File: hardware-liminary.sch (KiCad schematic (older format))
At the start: 51 parts, among them J1 Conn_01x05, J2 Conn_01x03, J3 Conn_01x03, J4 Conn_02x05_Odd_Even, J5 Conn_01x02, J6 UFL Conn, K1 HL2-1CH-12S, Q1 CMBT3904, Q2 PT204-6C, Q3 CMBT2222A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

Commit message: Asociadas footprint de componentes standard
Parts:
- AE1: footprint (none) -> Connector_Pin:Pin_D1.3mm_L11.0mm_LooseFit
- BAT1, J5, JP1: footprint (none) -> Connector_PinHeader_2.54mm:PinHeader_1x02_P2.54mm_Vertical
- C1: footprint (none) -> Capacitor_THT:CP_Radial_D5.0mm_P2.00mm
- C10: footprint (none) -> Capacitor_SMD:C_1206_3216Metric_Pad1.42x1.75mm_HandSolder
- C11, C12, C13, C2, C9: footprint (none) -> Capacitor_SMD:C_0805_2012Metric_Pad1.15x1.40mm_HandSolder
- C14, C3, C5, C6, C7, C8: footprint (none) -> Capacitor_SMD:CP_Elec_4x5.3
- C4: footprint (none) -> Capacitor_SMD:CP_Elec_4x5.4
- J1: footprint (none) -> Connector_PinHeader_2.54mm:PinHeader_1x05_P2.54mm_Vertical
- J2, J3: footprint (none) -> Connector_PinHeader_2.54mm:PinHeader_1x03_P2.54mm_Vertical
- J4: footprint (none) -> Connector_PinHeader_1.27mm:PinHeader_2x05_P1.27mm_Vertical
- J6: footprint TE_1909763-1 -> (none)
- K1: footprint Relay_THT:Relay_StandexMeder_DIP_LowProfile -> (none)
- LED1: footprint LED_SMD:LED_LiteOn_LTST-S326 -> (none)
- PS1: footprint Converter_ACDC:Converter_ACDC_MeanWell_IRM-03-xx_THT -> (none)
- Q1, Q3: footprint Package_TO_SOT_SMD:SOT-23 -> (none)
- Q2: footprint (none) -> LED_THT:LED_D5.0mm_Clear
- R1, R10, R11, R2, R3, R4, R5, R6, R7, R8, R9: footprint (none) -> Resistor_SMD:R_1206_3216Metric_Pad1.42x1.75mm_HandSolder
- RV1: footprint (none) -> Varistor:RV_Disc_D15.5mm_W3.9mm_P7.5mm
- U1: footprint lib:EESAMR34 -> (none)
- U2: footprint Package_TO_SOT_SMD:SOT-223-3_TabPin2 -> (none)

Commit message: eesam34
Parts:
- removed J6: UFL Conn, symbol 1909763-1:1909763-1
- removed LED1: 12-22/G6R6C-A31/2C, symbol LED_12-22:12-22SURSYGC_S530-A2_TR8
- removed U1: EESAMR34J18-V1_CT, symbol EESAMR34:EESAMR34J18-V1_CT
- removed U6: MCP6001T-I_OT, symbol MCP6001T-I_OT:MCP6001T-I_OT
- added U1: EESAMR34J18-V1_CT, proyect_EESAMR34:EESAMR34, symbol proyect_EESAMR34J18-V1_CT:EESAMR34J18-V1_CT
- JP3, JP4: footprint (none) -> Resistor_SMD:R_1206_3216Metric_Pad1.42x1.75mm_HandSolder
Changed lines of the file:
@@
 	3100 1350 3100 1250
-$Comp
-L MCP6001T-I_OT:MCP6001T-I_OT U6
-U 1 1 5F764C68
-P 3550 3500
-F 0 "U6" H 4150 3350 50  0000 C CNN
-F 1 "MCP6001T-I_OT" H 4150 3250 50  0000 C CNN
-F 2 "" H 4600 3900 50  0001 L CNN
-F 3 "http://docs-emea.rs-online.com/webdocs/0dd1/0900766b80dd189c.pdf" H 4600 3800 50  0001 L CNN
-F 4 "Single 1.8V Op Amp, 1MHz, I temp" H 4600 3700 50  0001 L CNN "Description"
-F 5 "1.45" H 4600 3600 50  0001 L CNN "Height"
-F 6 "Microchip" H 4600 3500 50  0001 L CNN "Manufacturer_Name"
-F 7 "MCP6001T-I/OT" H 4600 3400 50  0001 L CNN "Manufacturer_Part_Number"
-F 8 "MCP6001T-I/OT" H 4600 3300 50  0001 L CNN "Arrow Part Number"
-F 9 "https://www.arrow.com/en/products/mcp6001t-iot/microchip-technology" H 4600 3200 50  0001 L CNN "Arrow Price/Stock"
-F 10 "579-MCP6001T-I/OT" H 4600 3100 50  0001 L CNN "Mouser Part Number"
-F 11 "https://www.mouser.co.uk/ProductDetail/Microchip-Technology/MCP6001T-I-OT?qs=Q%2Fw7XRh99iki9dglS7IqJg%3D%3D" H 4600 3000 50  0001 L CNN "Mouser Price/Stock"
-	1    3550 3500
-	-1   0    0    -1
-$EndComp
 $Comp
 L Device:R R7
@@
 Wire Notes Line
 	5800 2400 500  2400
-$Comp
-L EESAMR34:EESAMR34J18-V1_CT U1
-U 1 1 5F95A58C
-P 2000 6650
-F 0 "U1" H 2150 6700 50  0000 R CNN
-F 1 "EESAMR34J18-V1_CT" H 2500 6550 50  0000 R CNN
-F 2 "" H 2000 6650 50  0001 L BNN
-F 3 "" H 2000 6650 118 0001 C CNN
-	1    2000 6650
-	1    0    0    -1
-$EndComp
 $Comp
 L power:GNDD #PWR0103
@@
 	1800 7650 1800 8150
 $Comp
-L LED_12-22:12-22SURSYGC_S530-A2_TR8 LED1
-U 1 1 5F8C80DF
-P 4500 8150
-F 0 "LED1" H 5000 8415 50  0000 C CNN
-F 1 "12-22/G6R6C-A31/2C" H 5000 8324 50  0000 C CNN
-F 2 "" H 5350 8250 50  0001 L CNN
-F 3 "" H 5350 8150 50  0001 L CNN
-F 4 "" H 5350 8050 50  0001 L CNN "Description"
-F 5 "2.2" H 5350 7950 50  0001 L CNN "Height"
-F 6 "Everlight" H 5350 7850 50  0001 L CNN "Manufacturer_Name"
-F 7 "12-22SURSYGC/S530-A2/TR8" H 5350 7750 50  0001 L CNN "Manufacturer_Part_Number"
-F 8 "12-22SURSYGC/S530-A2/TR8" H 5350 7650 50  0001 L CNN "Arrow Part Number"
-F 9 "" H 5350 7550 50  0001 L CNN "Arrow Price/Stock"
-F 10 "638-1222SURSYGCA2TR8" H 5350 7450 50  0001 L CNN "Mouser Part Number"
-F 11 "https://www.mouser.com/Search/Refine.aspx?Keyword=638-1222SURSYGCA2TR8" H 5350 7350 50  0001 L CNN "Mouser Price/Stock"
-	1    4500 8150
-	-1   0    0    -1
-$EndComp
-$Comp
 L Device:R R11
 U 1 1 5F8CC602
@@
 Antenna
 $Comp
-L 1909763-1:1909763-1 J6
-U 1 1 5FA17C3E
-P 6900 6000
-F 0 "J6" H 7188 6040 50  0000 L CNN
-F 1 "UFL Conn" H 7188 5949 50  0000 L CNN
-F 2 "" H 6900 6000 50  0001 L BNN
-F 3 "1909763-1" H 6900 6000 50  0001 L BNN
-F 4 "1" H 6900 6000 50  0001 L BNN "Field4"
-	1    6900 6000
-	1    0    0    -1
-$EndComp
-$Comp
 L power:GNDD #PWR014
 U 1 1 5FA23786
@@
 F 0 "JP4" H 6400 6164 50  0000 C CNN
 F 1 "Jumper" H 6400 6073 50  0000 C CNN
-F 2 "" H 6400 5900 50  0001 C CNN
+F 2 "Resistor_SMD:R_1206_3216Metric_Pad1.42x1.75mm_HandSolder" H 6400 5900 50  0001 C CNN
 F 3 "~" H 6400 5900 50  0001 C CNN
 	1    6400 5900
@@
 F 0 "JP3" H 6400 5814 50  0000 C CNN
 F 1 "Jumper" H 6400 5723 50  0000 C CNN
-F 2 "" H 6400 5550 50  0001 C CNN
+F 2 "Resistor_SMD:R_1206_3216Metric_Pad1.42x1.75mm_HandSolder" H 6400 5550 50  0001 C CNN
 F 3 "~" H 6400 5550 50  0001 C CNN
 	1    6400 5550
@@
 Wire Notes Line
 	7750 2350 7750 500
+$Comp
+L proyect_EESAMR34J18-V1_CT:EESAMR34J18-V1_CT U1
+U 1 1 5F767C93
+P 2000 6650
+F 0 "U1" H 1057 6646 50  0000 R CNN
+F 1 "EESAMR34J18-V1_CT" H 1057 6555 50  0000 R CNN
+F 2 "proyect_EESAMR34:EESAMR34" H 2000 6650 50  0001 L BNN
+F 3 "" H 2000 6650 50  0001 C CNN
+	1    2000 6650
+	1    0    0    -1
+$EndComp
 $EndSCHEMATC

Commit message: opAmp
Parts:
- added IC1: MCP6001T-I_OT, proyect_MCP6001T-I_OT:SOT95P270X145-5N, symbol proyect_MCP6001T-I_OT:MCP6001T-I_OT
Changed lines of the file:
@@
 	1    0    0    -1
 $EndComp
+$Comp
+L proyect_MCP6001T-I_OT:MCP6001T-I_OT IC1
+U 1 1 5F79C962
+P 3550 3500
+F 0 "IC1" H 4150 4281 50  0000 C CNN
+F 1 "MCP6001T-I_OT" H 4150 4190 50  0000 C CNN
+F 2 "proyect_MCP6001T-I_OT:SOT95P270X145-5N" H 4600 3900 50  0001 L CNN
+F 3 "http://docs-emea.rs-online.com/webdocs/0dd1/0900766b80dd189c.pdf" H 4600 3800 50  0001 L CNN
+F 4 "Single 1.8V Op Amp, 1MHz, I temp" H 4600 3700 50  0001 L CNN "Description"
+F 5 "1.45" H 4600 3600 50  0001 L CNN "Height"
+F 6 "Microchip" H 4600 3500 50  0001 L CNN "Manufacturer_Name"
+F 7 "MCP6001T-I/OT" H 4600 3400 50  0001 L CNN "Manufacturer_Part_Number"
+F 8 "MCP6001T-I/OT" H 4600 3300 50  0001 L CNN "Arrow Part Number"
+F 9 "https://www.arrow.com/en/products/mcp6001t-iot/microchip-technology" H 4600 3200 50  0001 L CNN "Arrow Price/Stock"
+F 10 "579-MCP6001T-I/OT" H 4600 3100 50  0001 L CNN "Mouser Part Number"
+F 11 "https://www.mouser.co.uk/ProductDetail/Microchip-Technology/MCP6001T-I-OT?qs=Q%2Fw7XRh99iki9dglS7IqJg%3D%3D" H 4600 3000 50  0001 L CNN "Mouser Price/Stock"
+	1    3550 3500
+	-1   0    0    -1
+$EndComp
 $EndSCHEMATC

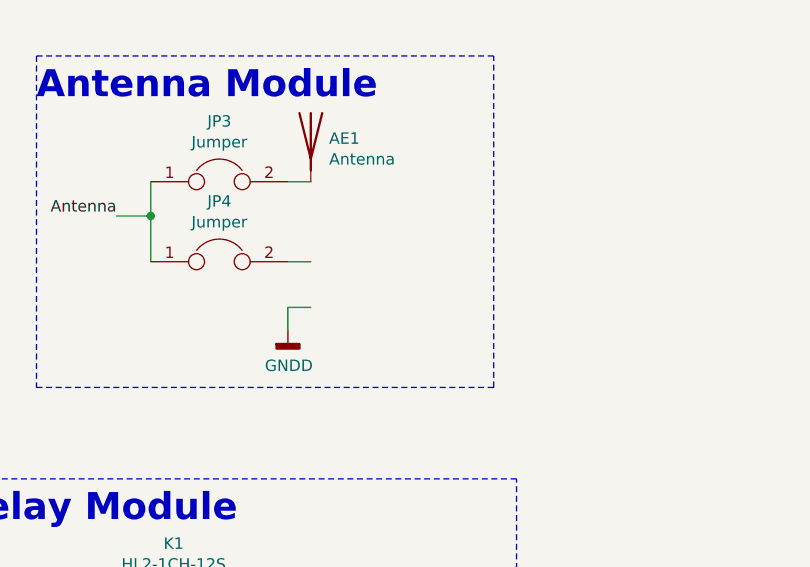
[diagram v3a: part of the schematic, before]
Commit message: ufl connector
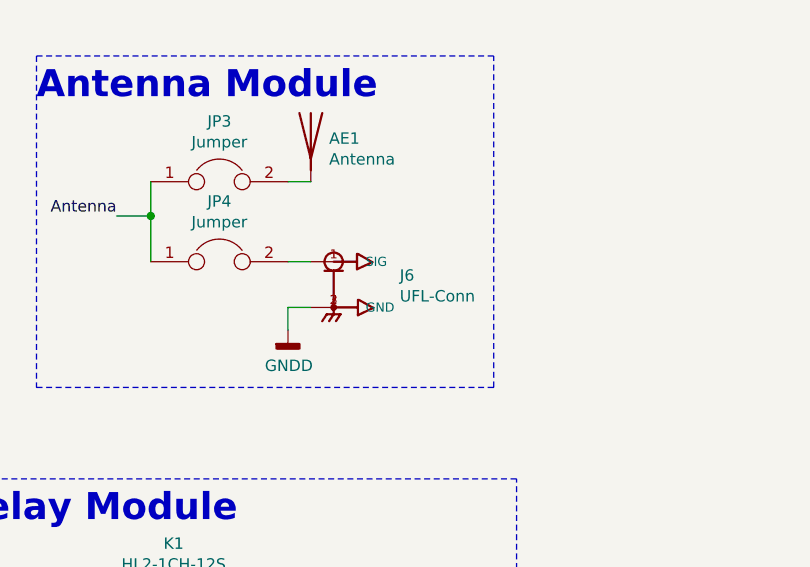
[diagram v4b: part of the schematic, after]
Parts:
- added J6: UFL-Conn, proyect_UFL-Conn:TE_1909763-1, symbol proyect_UFL-Conn:1909763-1
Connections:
- net GNDD: now also J6.2 (GND), J6.3 (GND)
- net at JP4.2: now also J6.1 (SIG)
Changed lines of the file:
@@
 	-1   0    0    -1
 $EndComp
+$Comp
+L proyect_UFL-Conn:1909763-1 J6
+U 1 1 5F7BE21B
+P 6900 6000
+F 0 "J6" H 7189 6040 50  0000 L CNN
+F 1 "UFL-Conn" H 7189 5949 50  0000 L CNN
+F 2 "proyect_UFL-Conn:TE_1909763-1" H 6900 6000 50  0001 L BNN
+F 3 "1909763-1" H 6900 6000 50  0001 L BNN
+F 4 "1" H 6900 6000 50  0001 L BNN "Field4"
+	1    6900 6000
+	1    0    0    -1
+$EndComp
 $EndSCHEMATC

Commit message: power supply
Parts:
- removed PS1: IRM-03-12, symbol Converter_ACDC:IRM-03-12
- added PS1: IRM-03-12, proyect_IRM-03-12:IRM0312, symbol proyect_IRM-03-12:IRM-03-12
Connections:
- net +12v: now also PS1.5 (+V)
- net GNDA: now also PS1.4 (-V)
- net Linea: now also PS1.1 (AC/L)
- net Neutro: now also PS1.2 (AC/N)
- no-connect marks 22 -> 24
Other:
- moved on the sheet: RV1
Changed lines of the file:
@@
 L Device:Varistor RV1
 U 1 1 5F736B9D
-P 3100 1100
-F 0 "RV1" H 2979 1054 50  0000 R CNN
-F 1 "Varistor" H 2979 1145 50  0000 R CNN
-F 2 "Varistor:RV_Disc_D15.5mm_W3.9mm_P7.5mm" V 3030 1100 50  0001 C CNN
-F 3 "~" H 3100 1100 50  0001 C CNN
-	1    3100 1100
+P 2450 1100
+F 0 "RV1" H 2329 1054 50  0000 R CNN
+F 1 "Varistor" H 2329 1145 50  0000 R CNN
+F 2 "Varistor:RV_Disc_D15.5mm_W3.9mm_P7.5mm" V 2380 1100 50  0001 C CNN
+F 3 "~" H 2450 1100 50  0001 C CNN
+	1    2450 1100
 	1    0    0    1
 $EndComp
@@
 Wire Wire Line
 	3400 2000 3400 2050
-Text Label 2700 850  2    50   ~ 0
+Text Label 2050 850  2    50   ~ 0
 Linea
-Text Label 2700 1350 2    50   ~ 0
+Text Label 2050 1350 2    50   ~ 0
 Neutro
 Wire Wire Line
-	2700 850  3100 850
-Wire Wire Line
-	3100 850  3100 950
-Wire Wire Line
-	2700 1350 3100 1350
-Wire Wire Line
-	3100 1350 3100 1250
+	2050 850  2450 850
+Wire Wire Line
+	2450 850  2450 950
+Wire Wire Line
+	2050 1350 2450 1350
+Wire Wire Line
+	2450 1350 2450 1250
 $Comp
 L Device:R R7
@@
 Wire Wire Line
 	4600 7700 4600 7800
-$Comp
-L Converter_ACDC:IRM-03-12 PS1
-U 1 1 5F9364C1
-P 3700 1100
-F 0 "PS1" H 3700 1467 50  0000 C CNN
-F 1 "IRM-03-12" H 3700 1376 50  0000 C CNN
-F 2 "" H 3700 750 50  0001 C CNN
-F 3 "https://www.meanwell.com/Upload/PDF/IRM-03/IRM-03-SPEC.PDF" H 3700 700 50  0001 C CNN
-	1    3700 1100
-	1    0    0    -1
-$EndComp
-Wire Wire Line
-	3300 1000 3300 850
-Wire Wire Line
-	3300 850  3100 850
-Connection ~ 3100 850
-Wire Wire Line
-	3300 1200 3300 1350
-Wire Wire Line
-	3300 1350 3100 1350
-Connection ~ 3100 1350
-Wire Wire Line
-	4100 1200 4100 1300
+Wire Wire Line
+	2650 850  2450 850
+Connection ~ 2450 850
+Wire Wire Line
+	2650 1350 2450 1350
+Connection ~ 2450 1350
 Wire Wire Line
 	4100 1300 4300 1300
 Connection ~ 4300 1300
-Wire Wire Line
-	4100 1000 4100 900
 Wire Wire Line
 	4100 900  4300 900
@@
 	1    0    0    -1
 $EndComp
+$Comp
+L proyect_IRM-03-12:IRM-03-12 PS1
+U 1 1 5F832713
+P 2900 950
+F 0 "PS1" H 3400 1215 50  0000 C CNN
+F 1 "IRM-03-12" H 3400 1124 50  0000 C CNN
+F 2 "proyect_IRM-03-12:IRM0312" H 3750 1050 50  0001 L CNN
+F 3 "https://www.meanwell-web.com/content/files/pdfs/productPdfs/MW/IRM-03/IRM-03-spec.pdf" H 3750 950 50  0001 L CNN
+F 4 "Mean Well 3W Encapsulated Switch Mode Power Supply, 0  250mA, 12V dc" H 3750 850 50  0001 L CNN "Description"
+F 5 "15" H 3750 750 50  0001 L CNN "Height"
+F 6 "Mean Well" H 3750 650 50  0001 L CNN "Manufacturer_Name"
+F 7 "IRM-03-12" H 3750 550 50  0001 L CNN "Manufacturer_Part_Number"
+F 8 "IRM-03-12" H 3750 450 50  0001 L CNN "Arrow Part Number"
+F 9 "https://www.arrow.com/en/products/irm-03-12/mean-well-enterprises" H 3750 350 50  0001 L CNN "Arrow Price/Stock"
+F 10 "709-IRM03-12" H 3750 250 50  0001 L CNN "Mouser Part Number"
+F 11 "https://www.mouser.co.uk/ProductDetail/MEAN-WELL/IRM-03-12?qs=NKmfXavxMawjMKY4aLDNfg%3D%3D" H 3750 150 50  0001 L CNN "Mouser Price/Stock"
+	1    2900 950
+	1    0    0    -1
+$EndComp
+NoConn ~ 3900 1050
+NoConn ~ 3900 1150
+Wire Wire Line
+	2650 850  2650 950
+Wire Wire Line
+	2650 950  2900 950
+Wire Wire Line
+	2650 1350 2650 1050
+Wire Wire Line
+	2650 1050 2900 1050
+Wire Wire Line
+	2900 1250 2900 1400
+Wire Wire Line
+	2900 1400 4100 1400
+Wire Wire Line
+	4100 1400 4100 1300
+Wire Wire Line
+	3900 950  4100 950
+Wire Wire Line
+	4100 950  4100 900
+$Comp
+L power:GNDA #PWR0114
+U 1 1 5F89AEDC
+P 9050 9950
+F 0 "#PWR0114" H 9050 9700 50  0001 C CNN
+F 1 "GNDA" H 9055 9777 50  0000 C CNN
+F 2 "" H 9050 9950 50  0001 C CNN
+F 3 "" H 9050 9950 50  0001 C CNN
+	1    9050 9950
+	1    0    0    -1
+$EndComp
+$Comp
+L power:PWR_FLAG #FLG0101
+U 1 1 5F89C39F
+P 9050 9950
+F 0 "#FLG0101" H 9050 10025 50  0001 C CNN
+F 1 "PWR_FLAG" H 9050 10123 50  0000 C CNN
+F 2 "" H 9050 9950 50  0001 C CNN
+F 3 "~" H 9050 9950 50  0001 C CNN
+	1    9050 9950
+	1    0    0    -1
+$EndComp
+Text Label 9850 9400 0    50   ~ 0
++12v
+$Comp
+L power:PWR_FLAG #FLG0105
+U 1 1 5F89CD25
+P 9850 9400
+F 0 "#FLG0105" H 9850 9475 50  0001 C CNN
+F 1 "PWR_FLAG" H 9850 9573 50  0000 C CNN
+F 2 "" H 9850 9400 50  0001 C CNN
+F 3 "~" H 9850 9400 50  0001 C CNN
+	1    9850 9400
+	-1   0    0    1
+$EndComp
 $EndSCHEMATC

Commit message: Leds
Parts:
- added LED1: 12-22SURSYGC_S530-A2_TR8, proyect_12-22_LEDs:1222SURSYGCS530A2TR8, symbol proyect_12-22_LEDs:12-22SURSYGC_S530-A2_TR8
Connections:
- net +3.3v: now also LED1.A1 (+)
- net at R11.2: now also LED1.C2 (-_2)
- net at R4.1: now also LED1.C1 (-_1)
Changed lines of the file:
@@
 	-1   0    0    1
 $EndComp
+$Comp
+L proyect_12-22_LEDs:12-22SURSYGC_S530-A2_TR8 LED1
+U 1 1 5F8A983B
+P 4500 8150
+F 0 "LED1" H 5000 8415 50  0000 C CNN
+F 1 "12-22SURSYGC_S530-A2_TR8" H 5000 8324 50  0000 C CNN
+F 2 "proyect_12-22_LEDs:1222SURSYGCS530A2TR8" H 5350 8250 50  0001 L CNN
+F 3 "https://componentsearchengine.com/Datasheets/1/12-22SURSYGC_S530-A2_TR8.pdf" H 5350 8150 50  0001 L CNN
+F 4 "LED Bi-Color Red/Yellow Green 632nm/575nm 3-Pin Chip LED T/R" H 5350 8050 50  0001 L CNN "Description"
+F 5 "2.2" H 5350 7950 50  0001 L CNN "Height"
+F 6 "Everlight" H 5350 7850 50  0001 L CNN "Manufacturer_Name"
+F 7 "12-22SURSYGC/S530-A2/TR8" H 5350 7750 50  0001 L CNN "Manufacturer_Part_Number"
+F 8 "12-22SURSYGC/S530-A2/TR8" H 5350 7650 50  0001 L CNN "Arrow Part Number"
+F 9 "" H 5350 7550 50  0001 L CNN "Arrow Price/Stock"
+F 10 "638-1222SURSYGCA2TR8" H 5350 7450 50  0001 L CNN "Mouser Part Number"
+F 11 "https://www.mouser.com/Search/Refine.aspx?Keyword=638-1222SURSYGCA2TR8" H 5350 7350 50  0001 L CNN "Mouser Price/Stock"
+	1    4500 8150
+	-1   0    0    -1
+$EndComp
 $EndSCHEMATC

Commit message: power supply 3D
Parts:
- PS1: footprint proyect_IRM-03-12:IRM0312 -> proyect_new:IRM0312
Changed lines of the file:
@@
 F 0 "PS1" H 3400 1215 50  0000 C CNN
 F 1 "IRM-03-12" H 3400 1124 50  0000 C CNN
-F 2 "proyect_IRM-03-12:IRM0312" H 3750 1050 50  0001 L CNN
+F 2 "proyect_new:IRM0312" H 3750 1050 50  0001 L CNN
 F 3 "https://www.meanwell-web.com/content/files/pdfs/productPdfs/MW/IRM-03/IRM-03-spec.pdf" H 3750 950 50  0001 L CNN
 F 4 "Mean Well 3W Encapsulated Switch Mode Power Supply, 0  250mA, 12V dc" H 3750 850 50  0001 L CNN "Description"

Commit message: power supply reemplazada por standard
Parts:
- removed PS1: IRM-03-12, proyect_new:IRM0312, symbol proyect_IRM-03-12:IRM-03-12
- added PS1: IRM-03-12, proyect_new:Converter_ACDC_MeanWell_IRM-03-xx_THT, symbol Converter_ACDC:IRM-03-12
- J4: value Conn_02x05_Odd_Even -> SWD
- J5: value Conn_01x02 -> Console
- LED1: value 12-22SURSYGC_S530-A2_TR8 -> 12-22/G6R6C-A31/2C
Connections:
- net +12v: now also PS1.16 (+Vo)
- net GNDA: now also PS1.14 (-Vo)
- net Linea: now also PS1.1 (AC/L)
- net Neutro: now also PS1.3 (AC/N)
- no-connect marks 24 -> 22
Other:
- moved on the sheet: RV1
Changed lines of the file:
@@
 L Device:Varistor RV1
 U 1 1 5F736B9D
-P 2450 1100
-F 0 "RV1" H 2329 1054 50  0000 R CNN
-F 1 "Varistor" H 2329 1145 50  0000 R CNN
-F 2 "Varistor:RV_Disc_D15.5mm_W3.9mm_P7.5mm" V 2380 1100 50  0001 C CNN
-F 3 "~" H 2450 1100 50  0001 C CNN
-	1    2450 1100
+P 2600 1100
+F 0 "RV1" H 2479 1054 50  0000 R CNN
+F 1 "Varistor" H 2479 1145 50  0000 R CNN
+F 2 "Varistor:RV_Disc_D15.5mm_W3.9mm_P7.5mm" V 2530 1100 50  0001 C CNN
+F 3 "~" H 2600 1100 50  0001 C CNN
+	1    2600 1100
 	1    0    0    1
 $EndComp
@@
 Wire Wire Line
 	3400 2000 3400 2050
-Text Label 2050 850  2    50   ~ 0
+Text Label 2200 850  2    50   ~ 0
 Linea
-Text Label 2050 1350 2    50   ~ 0
+Text Label 2200 1350 2    50   ~ 0
 Neutro
 Wire Wire Line
-	2050 850  2450 850
-Wire Wire Line
-	2450 850  2450 950
-Wire Wire Line
-	2050 1350 2450 1350
-Wire Wire Line
-	2450 1350 2450 1250
+	2200 850  2600 850
+Wire Wire Line
+	2600 850  2600 950
+Wire Wire Line
+	2200 1350 2600 1350
+Wire Wire Line
+	2600 1350 2600 1250
 $Comp
 L Device:R R7
@@
 P 1650 9700
 F 0 "J4" H 1700 10117 50  0000 C CNN
-F 1 "Conn_02x05_Odd_Even" H 1700 10026 50  0000 C CNN
+F 1 "SWD" H 1700 10026 50  0000 C CNN
 F 2 "Connector_PinHeader_1.27mm:PinHeader_2x05_P1.27mm_Vertical" H 1650 9700 50  0001 C CNN
 F 3 "~" H 1650 9700 50  0001 C CNN
@@
 P 1800 10400
 F 0 "J5" H 1718 10617 50  0000 C CNN
-F 1 "Conn_01x02" H 1718 10526 50  0000 C CNN
+F 1 "Console" H 1718 10526 50  0000 C CNN
 F 2 "Connector_PinHeader_2.54mm:PinHeader_1x02_P2.54mm_Vertical" H 1800 10400 50  0001 C CNN
 F 3 "~" H 1800 10400 50  0001 C CNN
@@
 Wire Wire Line
 	4600 7700 4600 7800
-Wire Wire Line
-	2650 850  2450 850
-Connection ~ 2450 850
-Wire Wire Line
-	2650 1350 2450 1350
-Connection ~ 2450 1350
-Wire Wire Line
-	4100 1300 4300 1300
+Connection ~ 2600 850
+Connection ~ 2600 1350
 Connection ~ 4300 1300
-Wire Wire Line
-	4100 900  4300 900
 Connection ~ 4300 900
 Wire Wire Line
@@
 U 1 1 5F767C93
 P 2000 6650
-F 0 "U1" H 1057 6646 50  0000 R CNN
-F 1 "EESAMR34J18-V1_CT" H 1057 6555 50  0000 R CNN
+F 0 "U1" H 2050 6650 50  0000 R CNN
+F 1 "EESAMR34J18-V1_CT" H 2450 6500 50  0000 R CNN
 F 2 "proyect_EESAMR34:EESAMR34" H 2000 6650 50  0001 L BNN
 F 3 "" H 2000 6650 50  0001 C CNN
@@
 U 1 1 5F79C962
 P 3550 3500
-F 0 "IC1" H 4150 4281 50  0000 C CNN
-F 1 "MCP6001T-I_OT" H 4150 4190 50  0000 C CNN
+F 0 "IC1" H 4150 3350 50  0000 C CNN
+F 1 "MCP6001T-I_OT" H 4150 3250 50  0000 C CNN
 F 2 "proyect_MCP6001T-I_OT:SOT95P270X145-5N" H 4600 3900 50  0001 L CNN
 F 3 "http://docs-emea.rs-online.com/webdocs/0dd1/0900766b80dd189c.pdf" H 4600 3800 50  0001 L CNN
@@
 $EndComp
 $Comp
-L proyect_IRM-03-12:IRM-03-12 PS1
-U 1 1 5F832713
-P 2900 950
-F 0 "PS1" H 3400 1215 50  0000 C CNN
-F 1 "IRM-03-12" H 3400 1124 50  0000 C CNN
-F 2 "proyect_new:IRM0312" H 3750 1050 50  0001 L CNN
-F 3 "https://www.meanwell-web.com/content/files/pdfs/productPdfs/MW/IRM-03/IRM-03-spec.pdf" H 3750 950 50  0001 L CNN
-F 4 "Mean Well 3W Encapsulated Switch Mode Power Supply, 0  250mA, 12V dc" H 3750 850 50  0001 L CNN "Description"
-F 5 "15" H 3750 750 50  0001 L CNN "Height"
-F 6 "Mean Well" H 3750 650 50  0001 L CNN "Manufacturer_Name"
-F 7 "IRM-03-12" H 3750 550 50  0001 L CNN "Manufacturer_Part_Number"
-F 8 "IRM-03-12" H 3750 450 50  0001 L CNN "Arrow Part Number"
-F 9 "https://www.arrow.com/en/products/irm-03-12/mean-well-enterprises" H 3750 350 50  0001 L CNN "Arrow Price/Stock"
-F 10 "709-IRM03-12" H 3750 250 50  0001 L CNN "Mouser Part Number"
-F 11 "https://www.mouser.co.uk/ProductDetail/MEAN-WELL/IRM-03-12?qs=NKmfXavxMawjMKY4aLDNfg%3D%3D" H 3750 150 50  0001 L CNN "Mouser Price/Stock"
-	1    2900 950
-	1    0    0    -1
-$EndComp
-NoConn ~ 3900 1050
-NoConn ~ 3900 1150
-Wire Wire Line
-	2650 850  2650 950
-Wire Wire Line
-	2650 950  2900 950
-Wire Wire Line
-	2650 1350 2650 1050
-Wire Wire Line
-	2650 1050 2900 1050
-Wire Wire Line
-	2900 1250 2900 1400
-Wire Wire Line
-	2900 1400 4100 1400
-Wire Wire Line
-	4100 1400 4100 1300
-Wire Wire Line
-	3900 950  4100 950
-Wire Wire Line
-	4100 950  4100 900
-$Comp
 L power:GNDA #PWR0114
 U 1 1 5F89AEDC
@@
 	1    0    0    -1
 $EndComp
-Text Label 9850 9400 0    50   ~ 0
-+12v
-$Comp
-L power:PWR_FLAG #FLG0105
-U 1 1 5F89CD25
-P 9850 9400
-F 0 "#FLG0105" H 9850 9475 50  0001 C CNN
-F 1 "PWR_FLAG" H 9850 9573 50  0000 C CNN
-F 2 "" H 9850 9400 50  0001 C CNN
-F 3 "~" H 9850 9400 50  0001 C CNN
-	1    9850 9400
-	-1   0    0    1
-$EndComp
 $Comp
 L proyect_12-22_LEDs:12-22SURSYGC_S530-A2_TR8 LED1
@@
 P 4500 8150
 F 0 "LED1" H 5000 8415 50  0000 C CNN
-F 1 "12-22SURSYGC_S530-A2_TR8" H 5000 8324 50  0000 C CNN
+F 1 "12-22/G6R6C-A31/2C" H 5000 8324 50  0000 C CNN
 F 2 "proyect_12-22_LEDs:1222SURSYGCS530A2TR8" H 5350 8250 50  0001 L CNN
 F 3 "https://componentsearchengine.com/Datasheets/1/12-22SURSYGC_S530-A2_TR8.pdf" H 5350 8150 50  0001 L CNN
@@
 	-1   0    0    -1
 $EndComp
+$Comp
+L Converter_ACDC:IRM-03-12 PS1
+U 1 1 5F7683F1
+P 3500 1100
+F 0 "PS1" H 3500 1467 50  0000 C CNN
+F 1 "IRM-03-12" H 3500 1376 50  0000 C CNN
+F 2 "proyect_new:Converter_ACDC_MeanWell_IRM-03-xx_THT" H 3500 750 50  0001 C CNN
+F 3 "https://www.meanwell.com/Upload/PDF/IRM-03/IRM-03-SPEC.PDF" H 3500 700 50  0001 C CNN
+	1    3500 1100
+	1    0    0    -1
+$EndComp
+Wire Wire Line
+	3900 1000 4000 1000
+Wire Wire Line
+	4000 1000 4000 900
+Wire Wire Line
+	4000 900  4300 900
+Wire Wire Line
+	3900 1200 4000 1200
+Wire Wire Line
+	4000 1200 4000 1300
+Wire Wire Line
+	4000 1300 4300 1300
+Wire Wire Line
+	3100 1000 3000 1000
+Wire Wire Line
+	3000 1000 3000 850
+Wire Wire Line
+	2600 850  3000 850
+Wire Wire Line
+	3000 1350 3000 1200
+Wire Wire Line
+	3000 1200 3100 1200
+Wire Wire Line
+	2600 1350 3000 1350
 $EndSCHEMATC
